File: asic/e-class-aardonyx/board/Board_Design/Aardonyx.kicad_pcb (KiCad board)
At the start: 4 copper layers, 157.5 x 117.3 mm, 329 parts, among them J1 Conn_1x4, J10 Conn_1x3_M, J11 Conn_1x8, J12 Conn_1x3_M, J13 USB_B_6PIN, J14 Conn_1x4, J15 Conn_1x3_M, J16 USB_OTG, J17 Conn_1x8, J18 Conn_1x3_M, J19 Conn_1x3_M, J2 Conn_1x6, J3 Conn_1x10_F, J4 Conn_1x8_F, J5 Conn_1x8_F, J6 Conn_1x6_F, J7 Conn_1x3_M, J8 PJ-202H PWRJACK, J9 Conn_1x6, Q1 FDN339AN, SW1 FSM2JSMAATR, SW2 SW_DIP_x03, SW3 SW_SPST, U1 LSF0108PWR, U10 ADM1186, U11 FT2232H, U12 TPS7A7002DDAR, U13 TPS54627DDAR, U14 93LC56BT-I_OT, U15 TPS7A7002DDAR, U2 SKT32E, U3 IS42S32160F-TSOP2, U4 LSF0108PWR, U5 CDCE913PW, U6 ADC128S102CIMTX/NOPB, U7 74AUP1G09GW, U8 IS25LP256x-xM, U9 CAT24M01WI-GT3, Y1 27MHz, Y2 12MHz

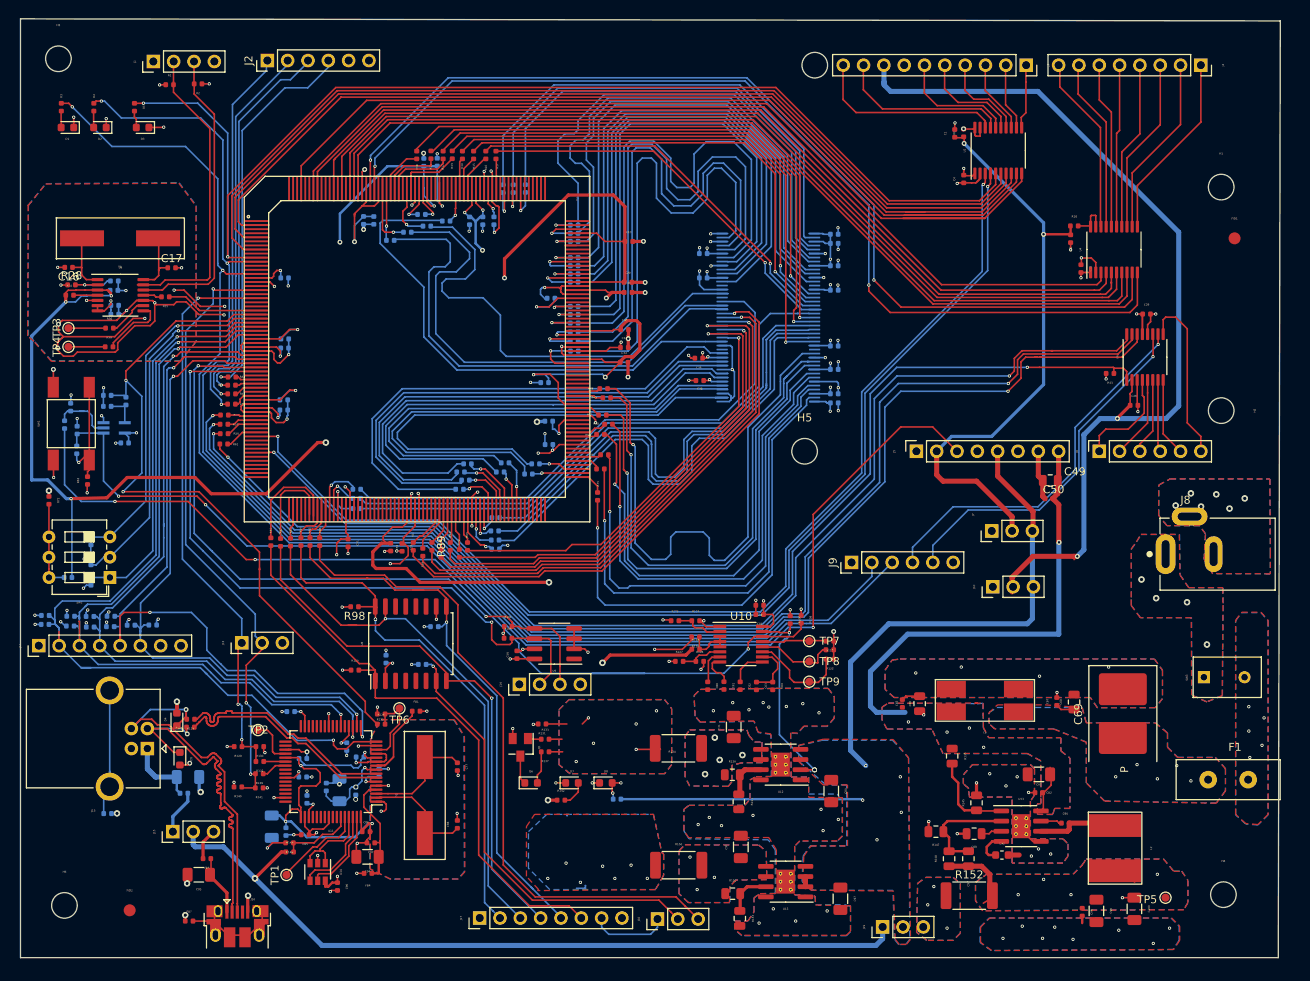
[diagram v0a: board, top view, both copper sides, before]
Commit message: updated silk screen
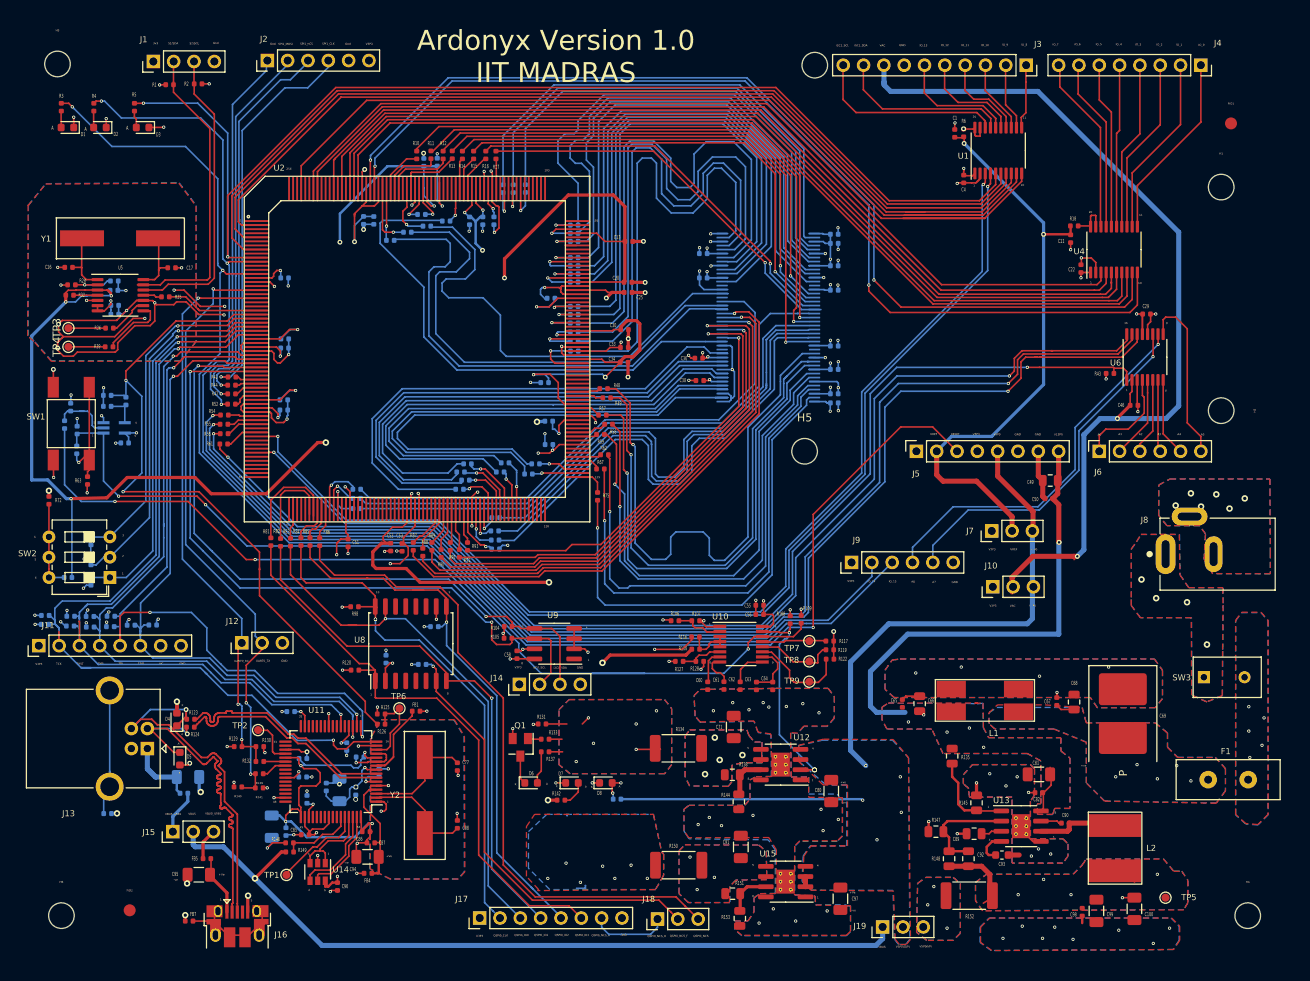
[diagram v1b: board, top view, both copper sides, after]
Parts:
- moved FID1 14.4 mm to (274.5, 58.3)
- moved H4 4.01 mm to (276.6, 157.3)
- moved H6 1.34 mm to (128.3, 157.3)
- moved H3 0.66 mm to (127.8, 50.9)
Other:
- board outline removed
- board text added: "+Ve"
- board text added: "+ve"
- board text added: "-Ve"
- board text added: "-ve"
- board text added: "1"
- board text added: "10"
- board text added: "11"
- board text added: "128"
- board text added: "129"
- board text added: "16"
- board text added: "17"
- board text added: "192"
- board text added: "193"
- board text added: "2"
- board text added: "20"
- board text added: "256"
- board text added: "3"
- board text added: "32"
- board text added: "33"
- board text added: "3v3"
- board text added: "4"
- board text added: "43"
- board text added: "44"
- board text added: "48"
- board text added: "49"
- board text added: "5"
- board text added: "6"
- board text added: "64"
- board text added: "65"
- board text added: "8"
- board text added: "86"
- board text added: "9"
- board text added: "A"
- board text added: "A0"
- board text added: "A1"
- board text added: "A2"
- board text added: "A3"
- board text added: "A4"
- board text added: "A5"
- board text added: "A6"
- board text added: "A7"
- board text added: "Ardonyx Version 1.0 IIT MADRAS"
- board text added: "GND"
- board text added: "Gnd"
- board text added: "I2C0_SCL"
- board text added: "I2C0_SDA"
- board text added: "I2C1_SCL"
- board text added: "IO_0"
- board text added: "IO_1"
- board text added: "IO_10"
- board text added: "IO_11"
- board text added: "IO_12"
- board text added: "IO_13"
- board text added: "IO_14"
- board text added: "IO_15"
- board text added: "IO_2"
- board text added: "IO_3"
- board text added: "IO_4"
- board text added: "IO_5"
- board text added: "IO_6"
- board text added: "IO_7"
- board text added: "IO_8"
- board text added: "IO_9"
- board text added: "ISC1_SDA"
- board text added: "K"
- board text added: "NC"
- board text added: "QSPI0_CLK"
- board text added: "QSPI0_IO0"
- board text added: "QSPI0_IO1"
- board text added: "QSPI0_IO2"
- board text added: "QSPI0_IO3"
- board text added: "QSPI0_NCS"
- board text added: "QSPI0_NCS_F"
- board text added: "QSPI0_NCS_H"
- board text added: "RESET"
- board text added: "S1/SDA"
- board text added: "S2/SCL"
- board text added: "SPI1_CLK"
- board text added: "SPI1_MOSI"
- board text added: "SPI1_nCS"
- board text added: "TCK"
- board text added: "TDI"
- board text added: "TDO"
- board text added: "TMS"
- board text added: "TRST"
- board text added: "UART0_RX"
- board text added: "UART0_TX"
- board text added: "V12P0"
- board text added: "V3P3"
- board text added: "V5P0"
- board text added: "V5P0(I/P)"
- board text added: "V5P0(O/P)"
- board text added: "VAC"
- board text added: "VBUS"
- board text added: "VBUS_USB1"
- board text added: "VBUS_USB2"
- board text added: "VREF"

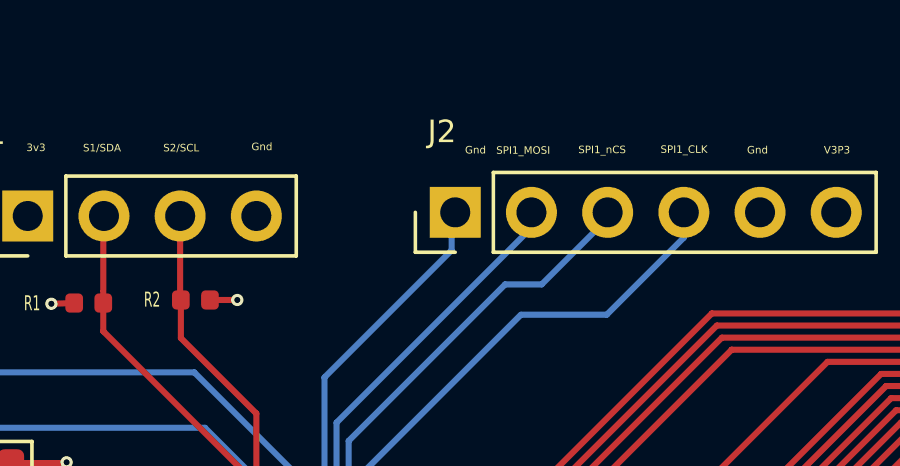
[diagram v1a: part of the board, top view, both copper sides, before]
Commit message: updated silkscreen
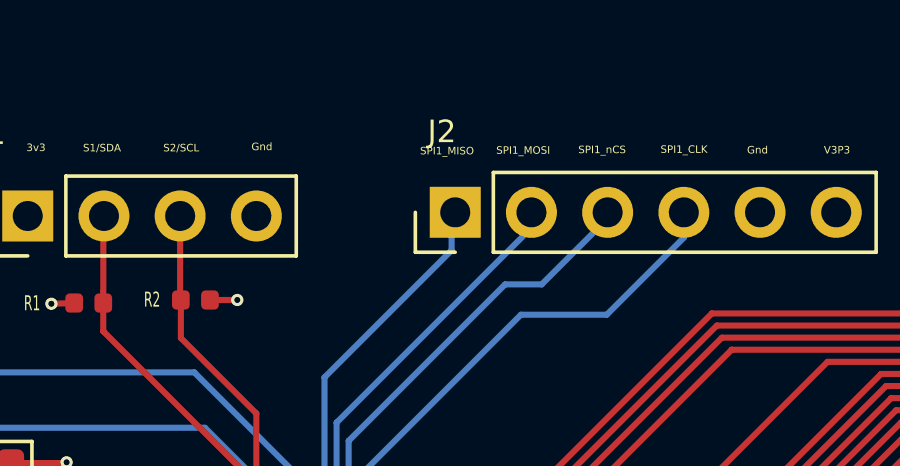
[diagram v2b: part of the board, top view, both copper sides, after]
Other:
- board text added: "SPI1_MISO"

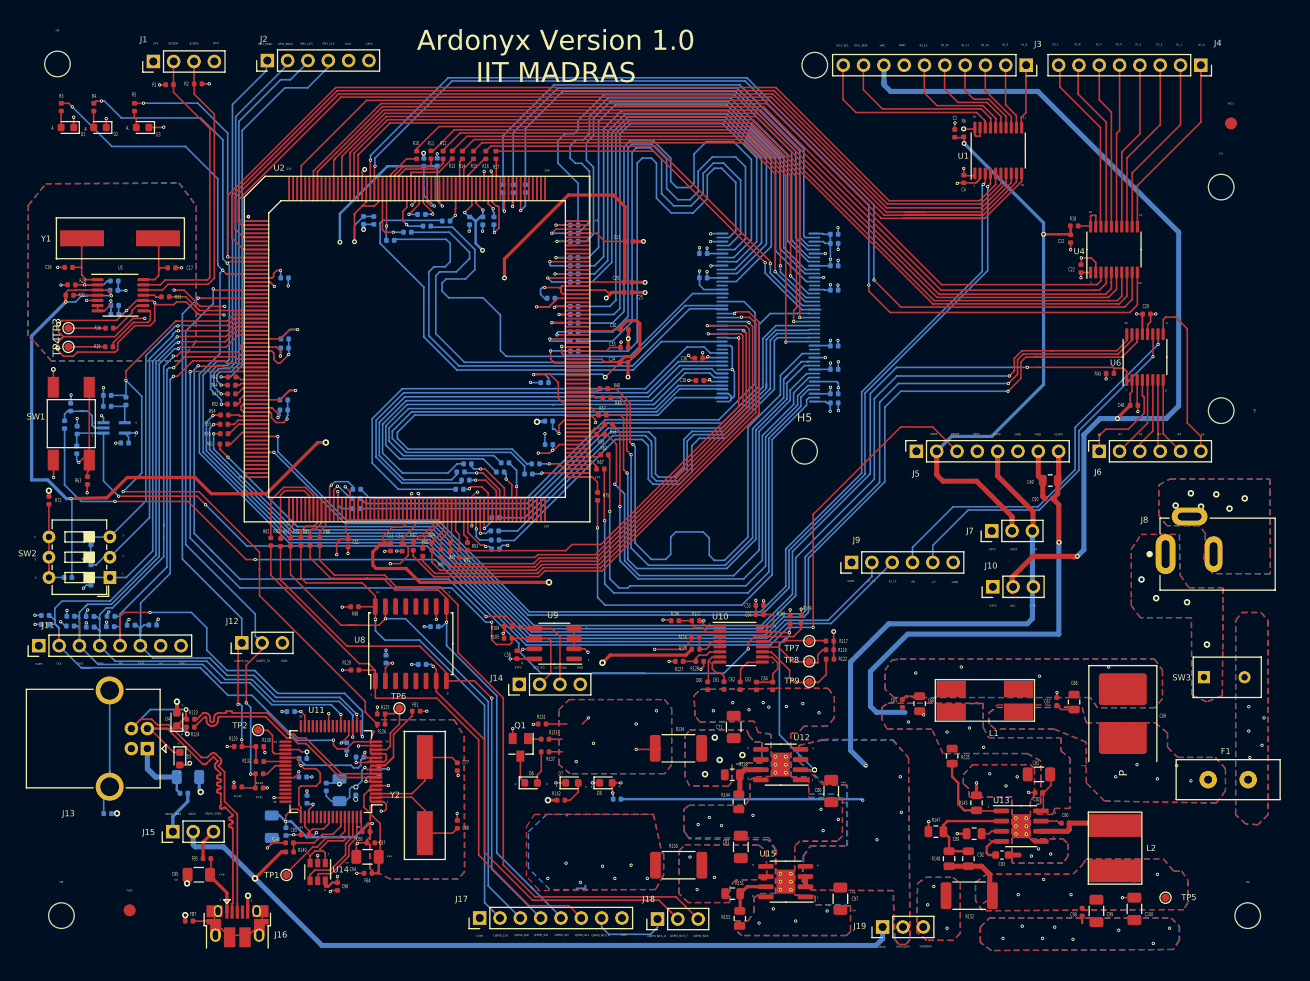
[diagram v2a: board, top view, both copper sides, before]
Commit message: updated silk screen
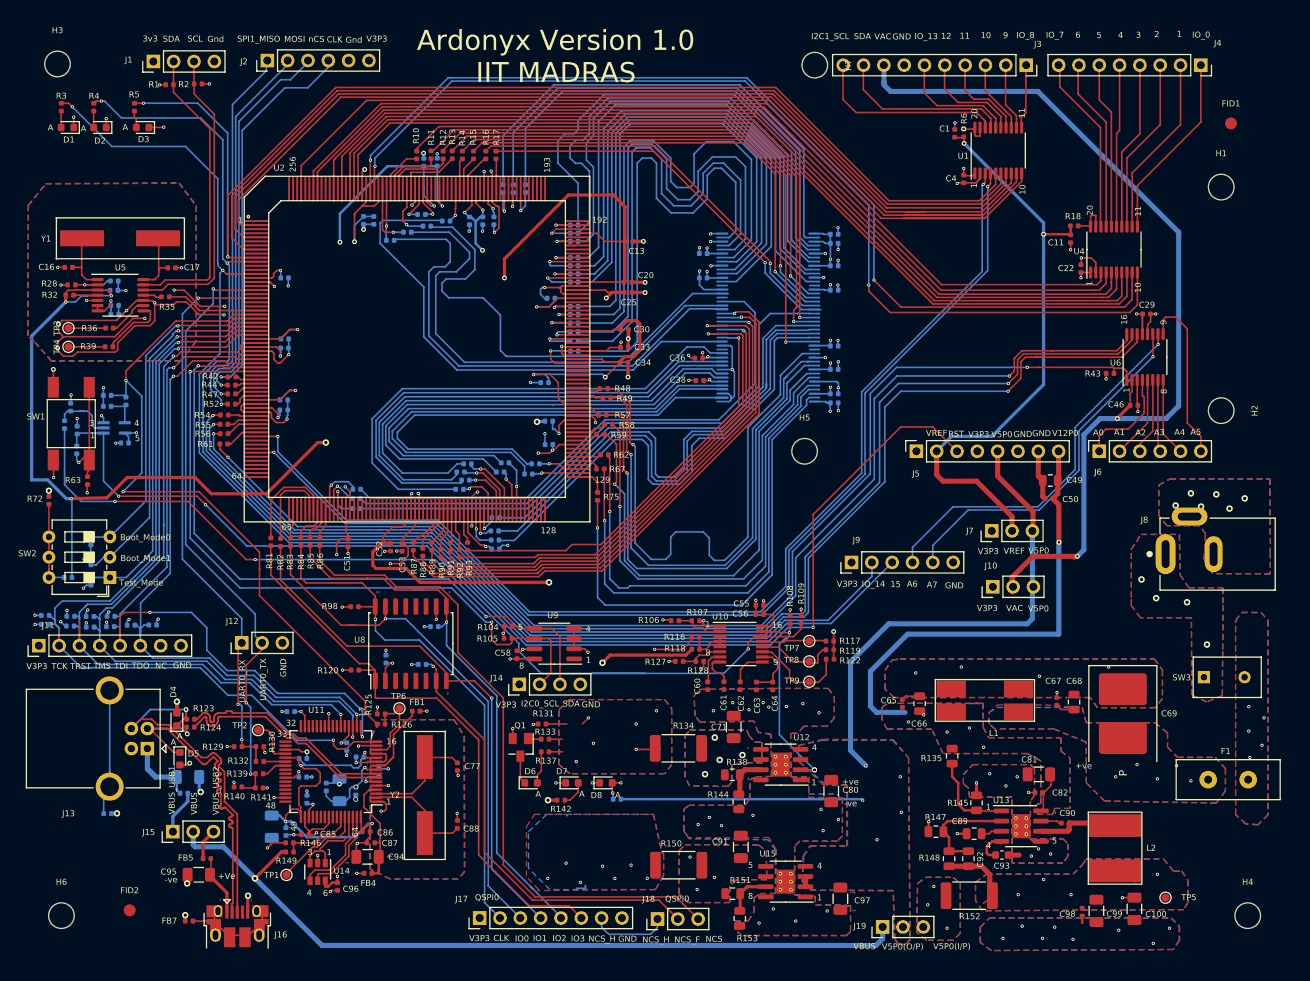
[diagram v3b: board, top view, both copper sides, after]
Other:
- board text added: "12"
- board text added: "15"
- board text added: "Boot_Mode0"
- board text added: "Boot_Mode1"
- board text added: "CLK"
- board text added: "IO0"
- board text added: "IO1"
- board text added: "IO2"
- board text added: "IO3"
- board text added: "MOSI"
- board text added: "NCS"
- board text added: "NCS_F"
- board text added: "NCS_H"
- board text added: "QSPI0"
- board text added: "RST"
- board text added: "SCL"
- board text added: "SDA"
- board text added: "Test_Mode"
- board text added: "nCS"
- board text removed: "I2C0_SDA"
- board text removed: "IO_1"
- board text removed: "IO_10"
- board text removed: "IO_11"
- board text removed: "IO_12"
- board text removed: "IO_15"
- board text removed: "IO_2"
- board text removed: "IO_3"
- board text removed: "IO_4"
- board text removed: "IO_5"
- board text removed: "IO_6"
- board text removed: "IO_9"
- board text removed: "ISC1_SDA"
- board text removed: "QSPI0_CLK"
- board text removed: "QSPI0_IO0"
- board text removed: "QSPI0_IO1"
- board text removed: "QSPI0_IO2"
- board text removed: "QSPI0_IO3"
- board text removed: "QSPI0_NCS"
- board text removed: "QSPI0_NCS_F"
- board text removed: "QSPI0_NCS_H"
- board text removed: "RESET"
- board text removed: "S1/SDA"
- board text removed: "S2/SCL"
- board text removed: "SPI1_CLK"
- board text removed: "SPI1_MOSI"
- board text removed: "SPI1_nCS"

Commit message: Updating power plane
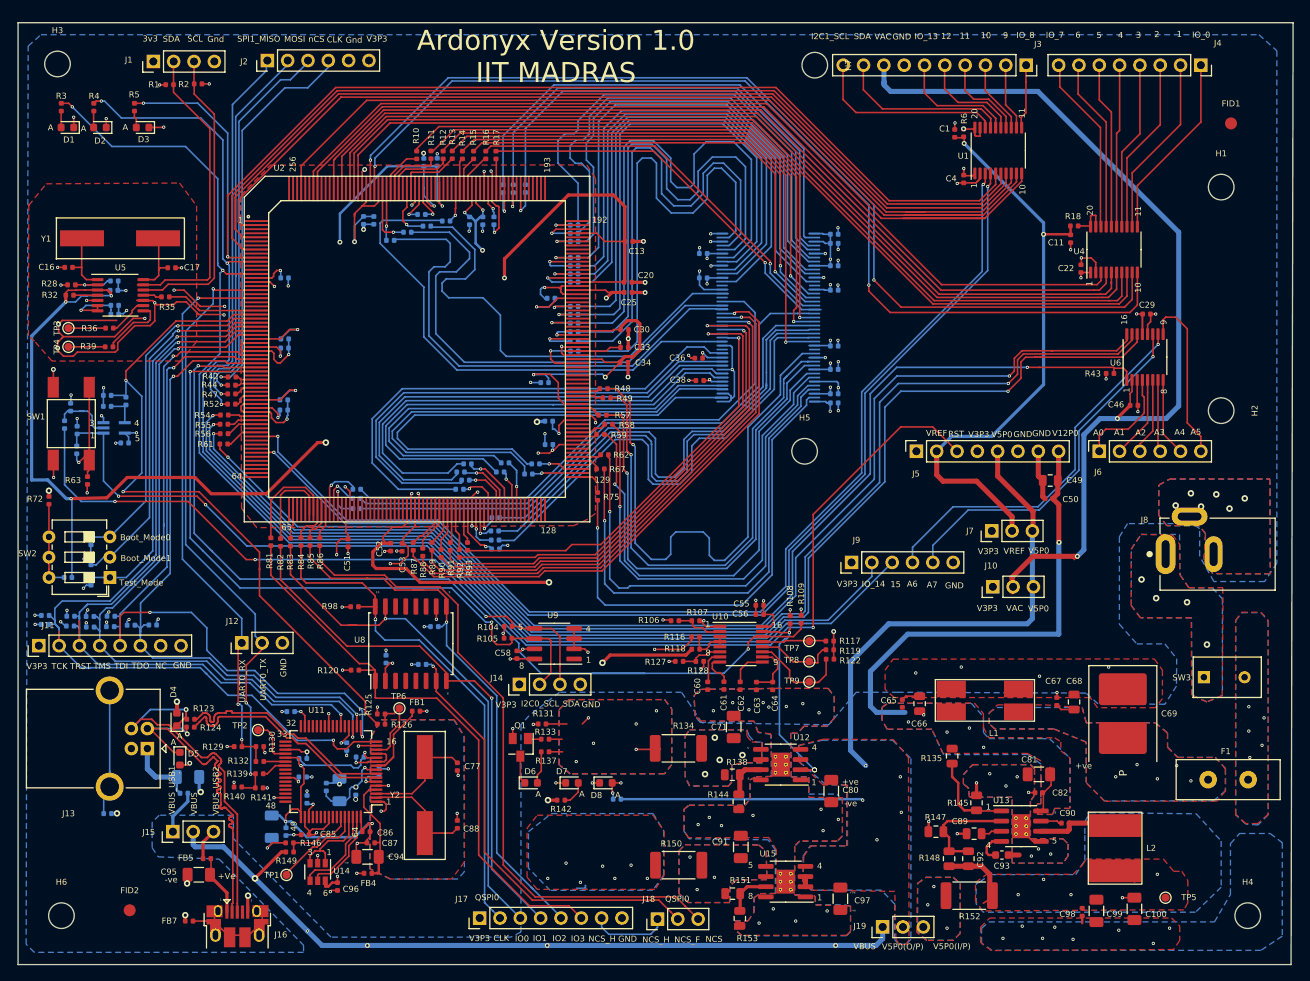
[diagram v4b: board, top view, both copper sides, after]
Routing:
- net VCORE_FTDI: track 50.9 -> 47.0 mm
- net GND: track 364.0 -> 360.5 mm
- net V3P3: track 188.7 -> 191.5 mm, vias 71 -> 70
- net VBUS: vias 1 -> 5
- added copper zone on In2.Cu, net VBUS
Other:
- board outline added: 159.4 x 117.7 mm
- rule trace_min: 0 -> 0.2032

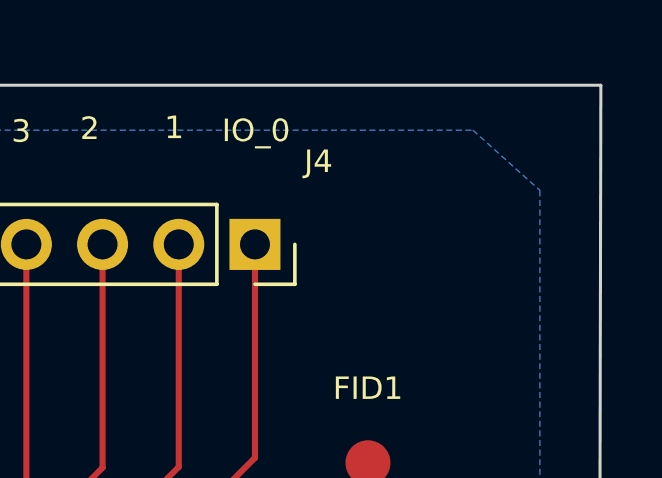
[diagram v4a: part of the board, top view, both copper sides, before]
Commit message: Adding Mounting hole
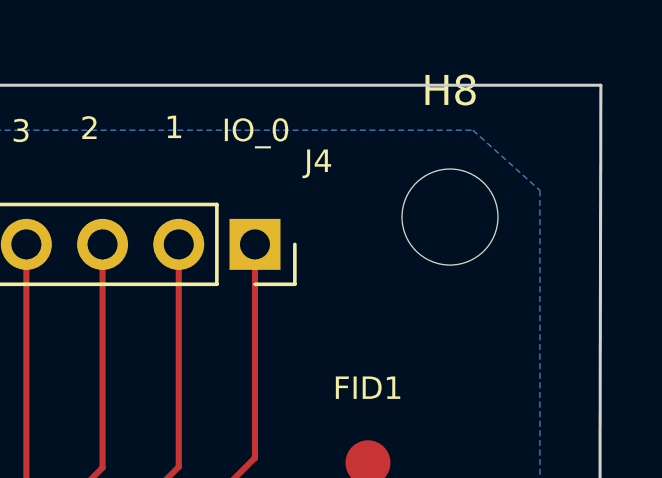
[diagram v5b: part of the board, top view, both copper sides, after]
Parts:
- added H8: MountingHole, MountingHole:MountingHole_3.2mm_M3, F.Cu at (277.2, 50.1)
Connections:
- SW3 pad 3: (no net) -> Net-(F1-Pad2)
